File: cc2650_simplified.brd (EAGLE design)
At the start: 50.7 x 23.1 mm, 13 parts, among them IC4 CC2650MODAMOHR, U402 TPS62233DRY

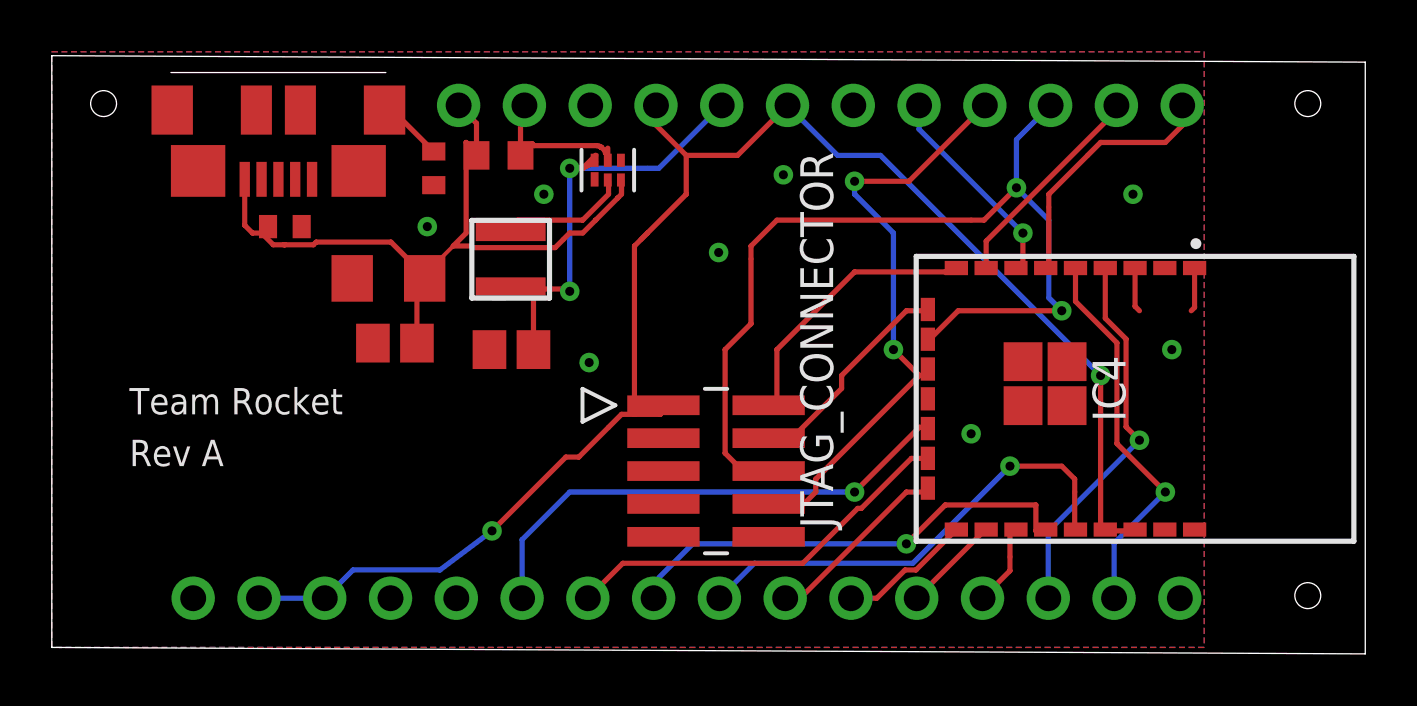
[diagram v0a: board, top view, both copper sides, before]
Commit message: fixed 1 wire and silkscreen
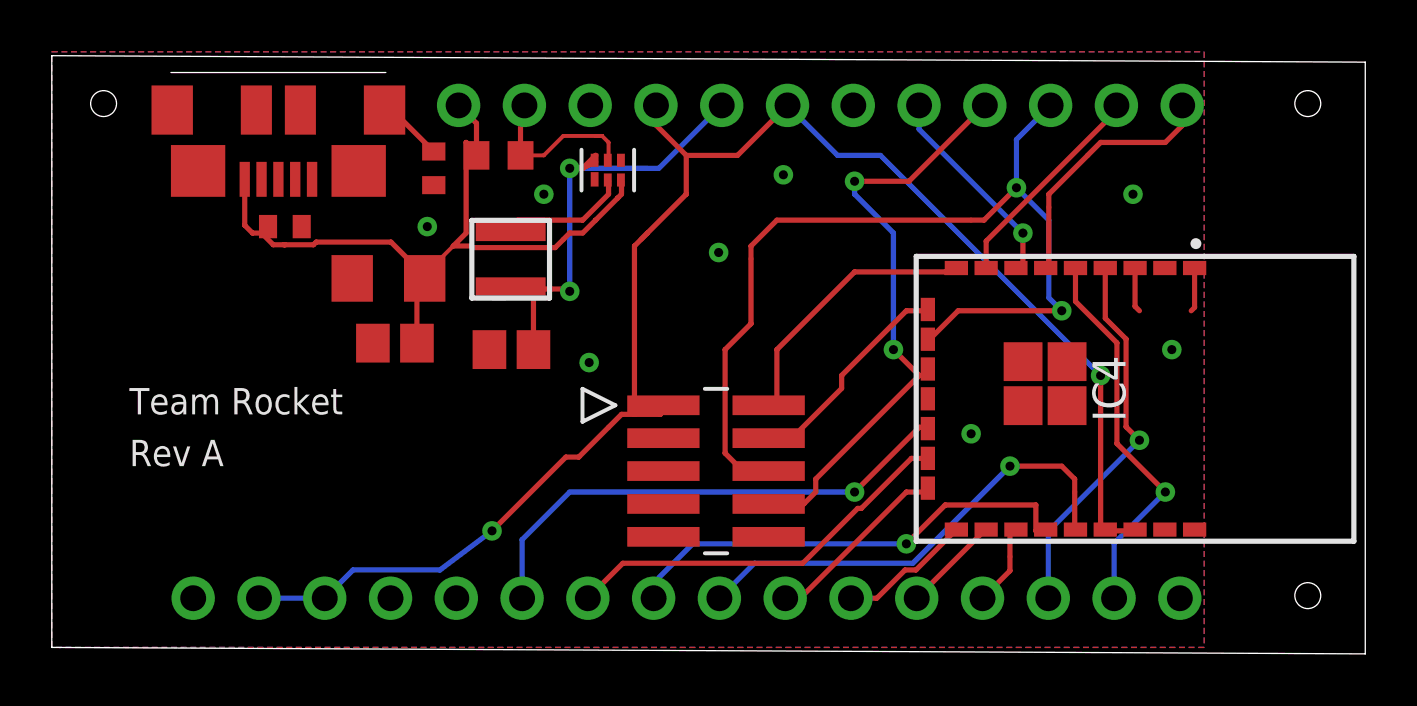
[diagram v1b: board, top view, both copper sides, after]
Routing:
- net EN: track 6.23 -> 6.76 mm
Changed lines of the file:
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@@
 <attribute name="SUPPLIER_NAME" value="RS" x="50.28" y="9.6" size="1.778" layer="27" rot="R270" display="off"/>
 </element>
-<element name="JTAG_CONNECTOR" library="FTSH-105-01-F-DV-K" package="SAMTEC_FTSH-105-01-L-DV" value="FTSH-105-01-F-DV-K" x="25.65" y="6.81" rot="R270">
+<element name="JTAG_CONNECTOR" library="FTSH-105-01-F-DV-K" package="SAMTEC_FTSH-105-01-L-DV" value="FTSH-105-01-F-DV-K" x="25.65" y="6.81" smashed="yes" rot="R270">
 <attribute name="3D_PACKAGE" value="" x="25.65" y="6.81" size="1.778" layer="27" rot="R270" display="off"/>
 <attribute name="ALLIED_NUMBER" value="" x="25.65" y="6.81" size="1.778" layer="27" rot="R270" display="off"/>
@@
 <attribute name="MF" value="" x="24.51" y="1.9" size="1.778" layer="28" rot="MR0" display="off"/>
 <attribute name="MPN" value="" x="24.51" y="1.9" size="1.778" layer="28" rot="MR0" display="off"/>
+<attribute name="NAME" x="44.9062" y="3.7288" size="0.8128" layer="26" ratio="18" rot="MR0"/>
 <attribute name="OC_NEWARK" value="unknown" x="24.51" y="1.9" size="1.778" layer="28" rot="MR0" display="off"/>
 <attribute name="VALUE" x="44.83" y="-1.275" size="0.4064" layer="28" ratio="10" rot="MR0"/>
@@
 <contactref element="U402" pad="5"/>
 <contactref element="R4" pad="2"/>
-<wire x1="21.47" y1="18.811" x2="21.47" y2="19" width="0.2" layer="1"/>
-<wire x1="21.47" y1="19" x2="21.47" y2="19.28" width="0.2" layer="1"/>
-<wire x1="18.55" y1="19.45" x2="18.1" y2="19" width="0.2" layer="1"/>
-<wire x1="21.3668" y1="19.16955" x2="21.21895" y2="19.3174" width="0.2" layer="1"/>
-<wire x1="21.21895" y1="19.3174" x2="21.214040625" y2="19.3174" width="0.2" layer="1"/>
-<wire x1="21.214040625" y1="19.3174" x2="21.213540625" y2="19.318153125" width="0.2" layer="1"/>
-<wire x1="21.213540625" y1="19.318153125" x2="21.17466875" y2="19.32596875" width="0.2" layer="1"/>
-<wire x1="21.17466875" y1="19.32596875" x2="21.1466375" y2="19.354" width="0.2" layer="1"/>
-<wire x1="21.375959375" y1="19.15578125" x2="21.3668" y2="19.16955" width="0.2" layer="1"/>
-<wire x1="21.47" y1="19" x2="21.375959375" y2="19.094040625" width="0.2" layer="1"/>
-<wire x1="21.375959375" y1="19.094040625" x2="21.375959375" y2="19.15578125" width="0.2" layer="1"/>
-<wire x1="18.624040625" y1="19.375959375" x2="18.55" y2="19.45" width="0.2" layer="1"/>
-<wire x1="21.1466375" y1="19.354" x2="21.0374125" y2="19.375959375" width="0.2" layer="1"/>
-<wire x1="21.0374125" y1="19.375959375" x2="18.624040625" y2="19.375959375" width="0.2" layer="1"/>
-<wire x1="18.1" y1="19" x2="18.1" y2="20.78" width="0.2" layer="1"/>
+<wire x1="18.1" y1="20.78" x2="18.1" y2="19" width="0.2" layer="1"/>
 <wire x1="18.1" y1="20.78" x2="18.25" y2="20.93" width="0.2" layer="1"/>
+<wire x1="18.1" y1="19" x2="19" y2="19" width="0.1524" layer="1"/>
+<wire x1="19" y1="19" x2="19.75" y2="19.75" width="0.1524" layer="1"/>
+<wire x1="19.75" y1="19.75" x2="21" y2="19.75" width="0.1524" layer="1"/>
+<wire x1="21" y1="19.75" x2="21.25" y2="19.75" width="0.1524" layer="1"/>
+<wire x1="21" y1="19.75" x2="21.25" y2="19.75" width="0.1524" layer="1"/>
+<wire x1="21.25" y1="19.75" x2="21.5" y2="19.5" width="0.1524" layer="1"/>
+<wire x1="21.5" y1="19.5" x2="21.5" y2="18.841" width="0.1524" layer="1"/>
+<wire x1="21.5" y1="18.841" x2="21.47" y2="18.811" width="0.1524" layer="1"/>
 </signal>
 <signal name="VBUS" class="2">
